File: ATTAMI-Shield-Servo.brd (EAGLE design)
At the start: 22.8 x 38.1 mm, 20 parts

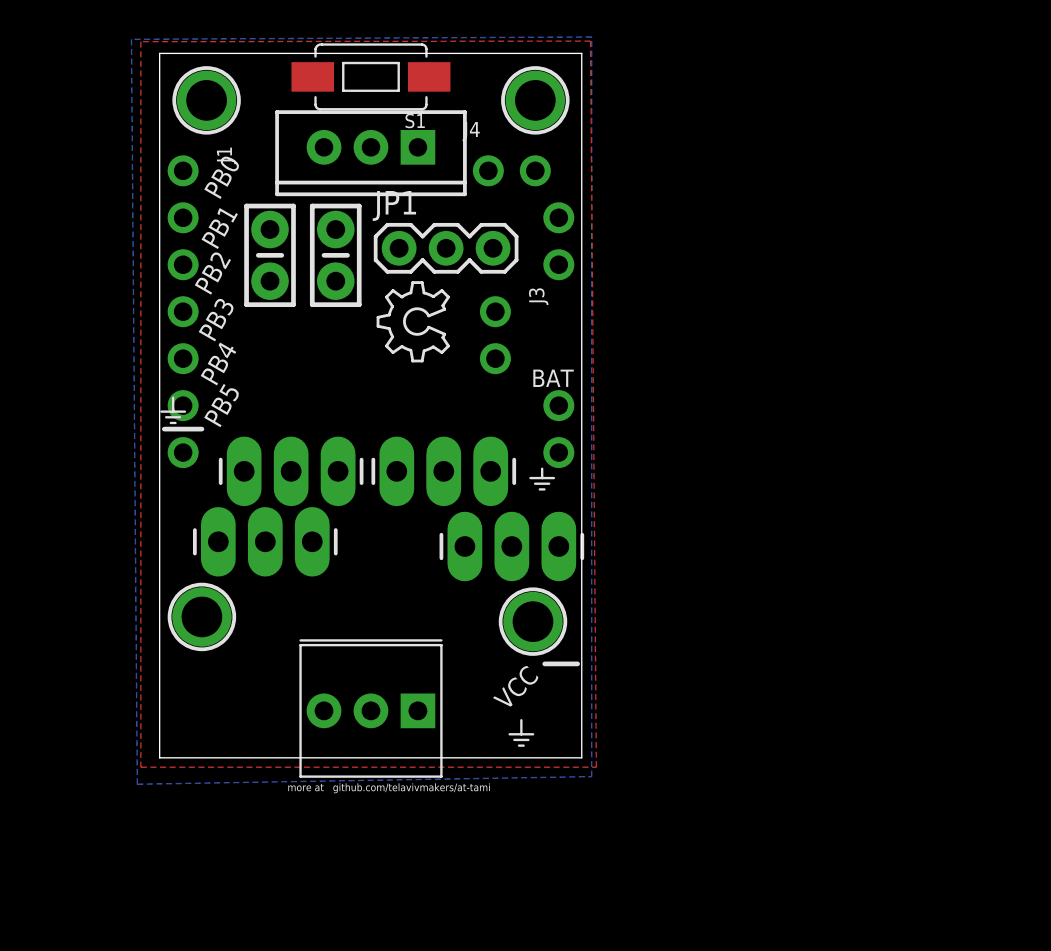
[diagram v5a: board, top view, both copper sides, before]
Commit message: midnight edition, 1x2 layout
taking space of two ATTami (1800x900 mil) .
leaving much place for silkscreen.
power on the right, servos on the left
no VCC pins on shield.
bottom copper plate is no longer ground, its now V_BAT.
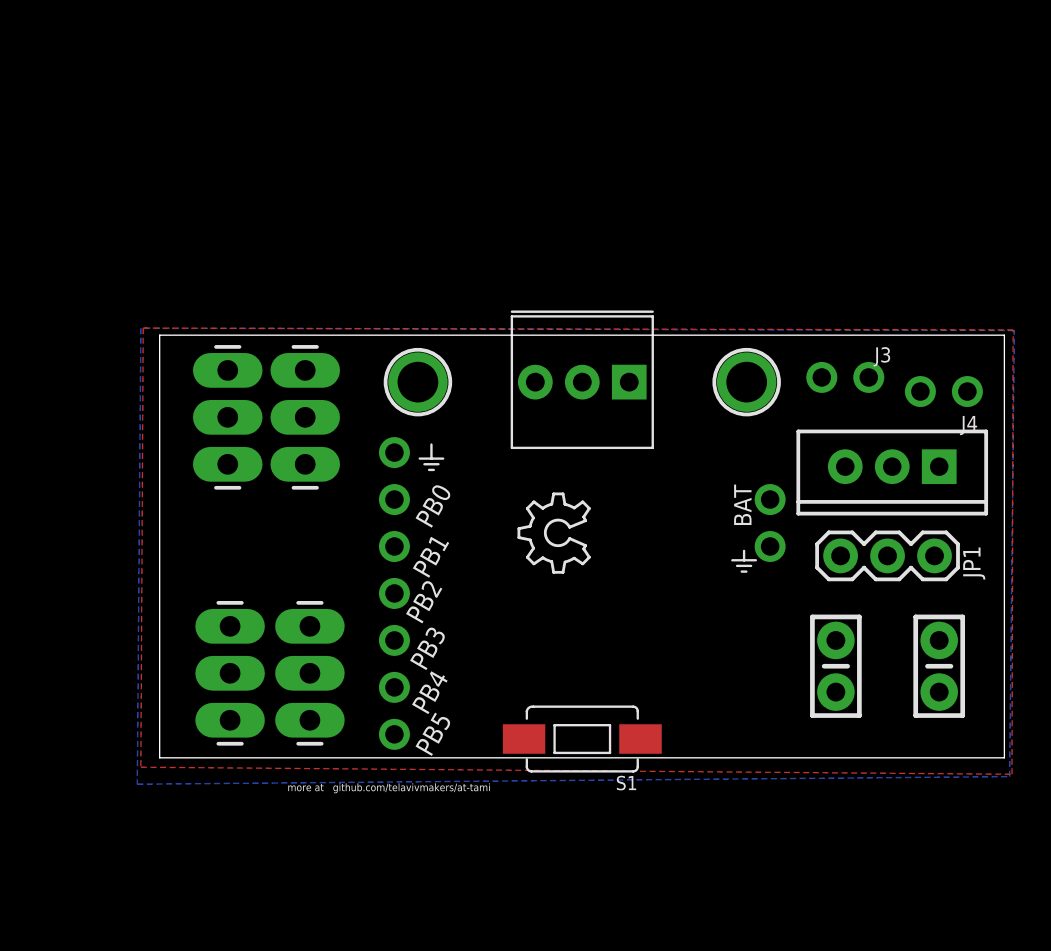
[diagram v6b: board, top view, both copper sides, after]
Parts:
- removed J5: (no value), microbuilder:1X02_ROUND
- removed U$4, U$5: MOUNTINGHOLE2.0, microbuilder:MOUNTINGHOLE_2.0_PLATED
- moved C2 42.5 mm to (42.2, 4.95), turned to 270 degrees
- moved S1 37.6 mm to (22.9, 1.02)
- moved C1 35.0 mm to (36.6, 4.95), turned to 270 degrees
- moved IC1 33.1 mm to (39.6, 15.7)
- moved JP1 29.1 mm to (36.8, 10.9)
- moved J4 26.2 mm to (42.4, 19.8), turned to 180 degrees
- moved POT 21.1 mm to (25.4, 22.9)
- moved J3 19.1 mm to (37.1, 20.6), turned to 0 degrees
- moved J2 19.1 mm to (33.0, 12.7)
- moved U$1 19.1 mm to (14.0, 20.3)
- moved U$2 19.1 mm to (31.8, 20.3)
- moved J1 19.0 mm to (12.7, 8.89)
- moved JP2 16.4 mm to (3.81, 7.11), turned to 270 degrees
- moved JP4 14.1 mm to (8.13, 7.11), turned to 270 degrees
- moved U$3 13.7 mm to (23.2, 10.0)
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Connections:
- new net N$1: IC1.IN, J4.1
- net GND: no longer J5.2
- net N$3: now also JP1.3; no longer JP1.1
- net VCC: no longer J5.1
- net V_IN: now also JP1.1; no longer IC1.IN, J4.1, JP1.3
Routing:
- added copper zone on layer 16, net V_BAT
- removed copper zone on layer 16, net GND
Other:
- board size 22.8 x 38.1 mm -> 45.7 x 22.9 mm

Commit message: rough layout change
switched position of servos for better layout
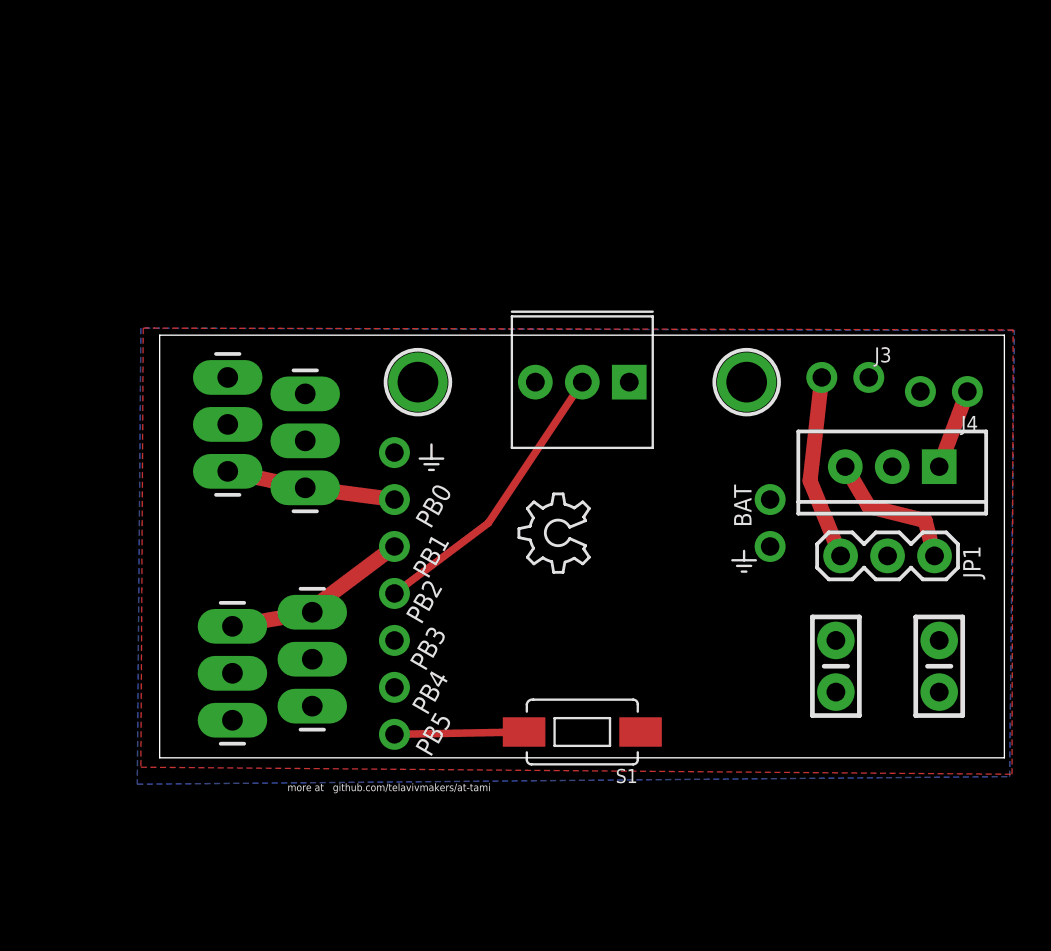
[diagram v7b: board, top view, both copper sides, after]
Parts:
- moved JP5 19.3 mm to (3.94, 2.03), turned to 90 degrees
- moved JP3 18.7 mm to (8.26, 2.79), turned to 90 degrees
- moved JP2 13.5 mm to (3.68, 20.6)
- moved JP4 12.6 mm to (7.87, 19.7)
- moved S1 0.38 mm to (22.9, 1.40)
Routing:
- net PB2(ADC1\SCK): track 0.00 -> 15.5 mm
- net PB1(MISO,PWM): track 0.00 -> 11.4 mm
- net V_IN: track 0.00 -> 10.0 mm
- net PB0(MOSI,PWM): track 0.00 -> 9.15 mm
- net N$3: track 0.00 -> 7.62 mm
- net PB5(RESET): track 0.00 -> 7.01 mm
- net N$1: track 0.00 -> 4.34 mm
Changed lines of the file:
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@@
 </element>
 <element name="U$3" library="ohw-logo" package="OSHW_6X150_NOTEXT" value="" x="23.241" y="10.033" rot="R90"/>
-<element name="JP2" library="SparkFun-Connectors" package="1X03_LONGPADS" value="servo1" x="3.81" y="7.112" smashed="yes" rot="R270">
-<attribute name="VALUE" x="0" y="8.382" size="1.27" layer="27" rot="R270"/>
+<element name="JP2" library="SparkFun-Connectors" package="1X03_LONGPADS" value="servo1" x="3.683" y="20.574" smashed="yes" rot="R270">
+<attribute name="VALUE" x="-0.127" y="21.844" size="1.27" layer="27" rot="R270"/>
 </element>
-<element name="JP3" library="SparkFun-Connectors" package="1X03_LONGPADS" value="servo2" x="3.683" y="20.955" smashed="yes" rot="R270">
-<attribute name="VALUE" x="-0.127" y="22.225" size="1.27" layer="27" rot="R270"/>
+<element name="JP3" library="SparkFun-Connectors" package="1X03_LONGPADS" value="servo2" x="8.255" y="2.794" smashed="yes" rot="R90">
+<attribute name="VALUE" x="12.065" y="1.524" size="1.27" layer="27" rot="R90"/>
 </element>
 <element name="IC1" library="SparkFun-PowerIC" package="TO220-IGO" value="" x="39.624" y="15.748" smashed="yes" rot="R180"/>
@@
 <attribute name="VALUE" x="44.958" y="22.987" size="0.4064" layer="27" ratio="10" rot="R180"/>
 </element>
-<element name="JP4" library="SparkFun-Connectors" package="1X03_LONGPADS" value="servo1_mirror" x="8.128" y="7.112" smashed="yes" rot="R270">
-<attribute name="VALUE" x="4.318" y="8.382" size="1.27" layer="27" rot="R270"/>
+<element name="JP4" library="SparkFun-Connectors" package="1X03_LONGPADS" value="servo1_mirror" x="7.874" y="19.685" smashed="yes" rot="R270">
+<attribute name="VALUE" x="4.064" y="20.955" size="1.27" layer="27" rot="R270"/>
 </element>
-<element name="JP5" library="SparkFun-Connectors" package="1X03_LONGPADS" value="servo2_mirror" x="7.874" y="20.955" smashed="yes" rot="R270">
-<attribute name="VALUE" x="4.064" y="22.225" size="1.27" layer="27" rot="R270"/>
+<element name="JP5" library="SparkFun-Connectors" package="1X03_LONGPADS" value="servo2_mirror" x="3.937" y="2.032" smashed="yes" rot="R90">
+<attribute name="VALUE" x="7.747" y="0.762" size="1.27" layer="27" rot="R90"/>
 </element>
-<element name="S1" library="SparkFun-Electromechanical" package="TACTILE-SWITCH-1101NE" value="SWITCH-MOMENTARY-2-SMD-1101NE" x="22.86" y="1.016" rot="R180"/>
+<element name="S1" library="SparkFun-Electromechanical" package="TACTILE-SWITCH-1101NE" value="SWITCH-MOMENTARY-2-SMD-1101NE" x="22.86" y="1.397" rot="R180"/>
 </elements>
 <signals>
@@
 <contactref element="J1" pad="2"/>
 <contactref element="JP4" pad="3"/>
-<wire x1="8.128" y1="2.032" x2="12.7" y2="13.97" width="0" layer="19" extent="1-1"/>
-<wire x1="3.81" y1="2.032" x2="8.128" y2="2.032" width="0" layer="19" extent="1-1"/>
+<wire x1="12.7" y1="13.97" x2="7.874" y2="14.605" width="0.8128" layer="1"/>
+<wire x1="7.874" y1="14.605" x2="3.683" y2="15.494" width="0.8128" layer="1"/>
 </signal>
 <signal name="PB1(MISO,PWM)">
@@
 <contactref element="J1" pad="3"/>
 <contactref element="JP5" pad="3"/>
-<wire x1="7.874" y1="15.875" x2="12.7" y2="11.43" width="0" layer="19" extent="1-1"/>
-<wire x1="3.683" y1="15.875" x2="7.874" y2="15.875" width="0" layer="19" extent="1-1"/>
+<wire x1="12.7" y1="11.43" x2="7.62" y2="7.62" width="0.8128" layer="1"/>
+<wire x1="7.62" y1="7.62" x2="8.255" y2="7.874" width="0.8128" layer="1"/>
+<wire x1="8.255" y1="7.874" x2="3.937" y2="7.112" width="0.8128" layer="1"/>
 </signal>
 <signal name="PB2(ADC1\SCK)">
 <contactref element="J1" pad="4"/>
 <contactref element="POT" pad="P$2"/>
-<wire x1="12.7" y1="8.89" x2="22.86" y2="20.32" width="0" layer="19" extent="1-1"/>
+<wire x1="22.86" y1="20.32" x2="17.78" y2="12.7" width="0.4064" layer="1"/>
+<wire x1="17.78" y1="12.7" x2="12.7" y2="8.89" width="0.4064" layer="1"/>
 </signal>
 <signal name="PB3(ADC3)">
@@
 <contactref element="J1" pad="7"/>
 <contactref element="S1" pad="P$2"/>
-<wire x1="12.7" y1="1.27" x2="19.71" y2="1.016" width="0" layer="19" extent="1-1"/>
+<wire x1="19.71" y1="1.397" x2="12.7" y2="1.27" width="0.4064" layer="1"/>
 </signal>
 <signal name="V_IN">
 <contactref element="J3" pad="1"/>
 <contactref element="JP1" pad="1"/>
-<wire x1="36.83" y1="10.922" x2="35.814" y2="20.574" width="0" layer="19" extent="1-1"/>
+<wire x1="35.814" y1="20.574" x2="35.179" y2="14.986" width="0.8128" layer="1"/>
+<wire x1="35.179" y1="14.986" x2="36.83" y2="10.922" width="0.8128" layer="1"/>
 </signal>
 <signal name="N$1">
 <contactref element="IC1" pad="IN"/>
 <contactref element="J4" pad="1"/>
-<wire x1="42.164" y1="15.748" x2="43.688" y2="19.812" width="0" layer="19" extent="1-1"/>
+<wire x1="43.688" y1="19.812" x2="42.164" y2="15.748" width="0.8128" layer="1"/>
 </signal>
 <signal name="N$3">
 <contactref element="IC1" pad="OUT"/>
 <contactref element="JP1" pad="3"/>
-<wire x1="41.91" y1="10.922" x2="37.084" y2="15.748" width="0" layer="19" extent="1-1"/>
+<wire x1="37.084" y1="15.748" x2="38.354" y2="13.589" width="0.8128" layer="1"/>
+<wire x1="38.354" y1="13.589" x2="41.402" y2="12.827" width="0.8128" layer="1"/>
+<wire x1="41.402" y1="12.827" x2="41.91" y2="10.922" width="0.8128" layer="1"/>
 </signal>
 </signals>
